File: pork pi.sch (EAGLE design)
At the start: 27 parts, among them J1 SJ-2523-SMT-TR, U1 A13

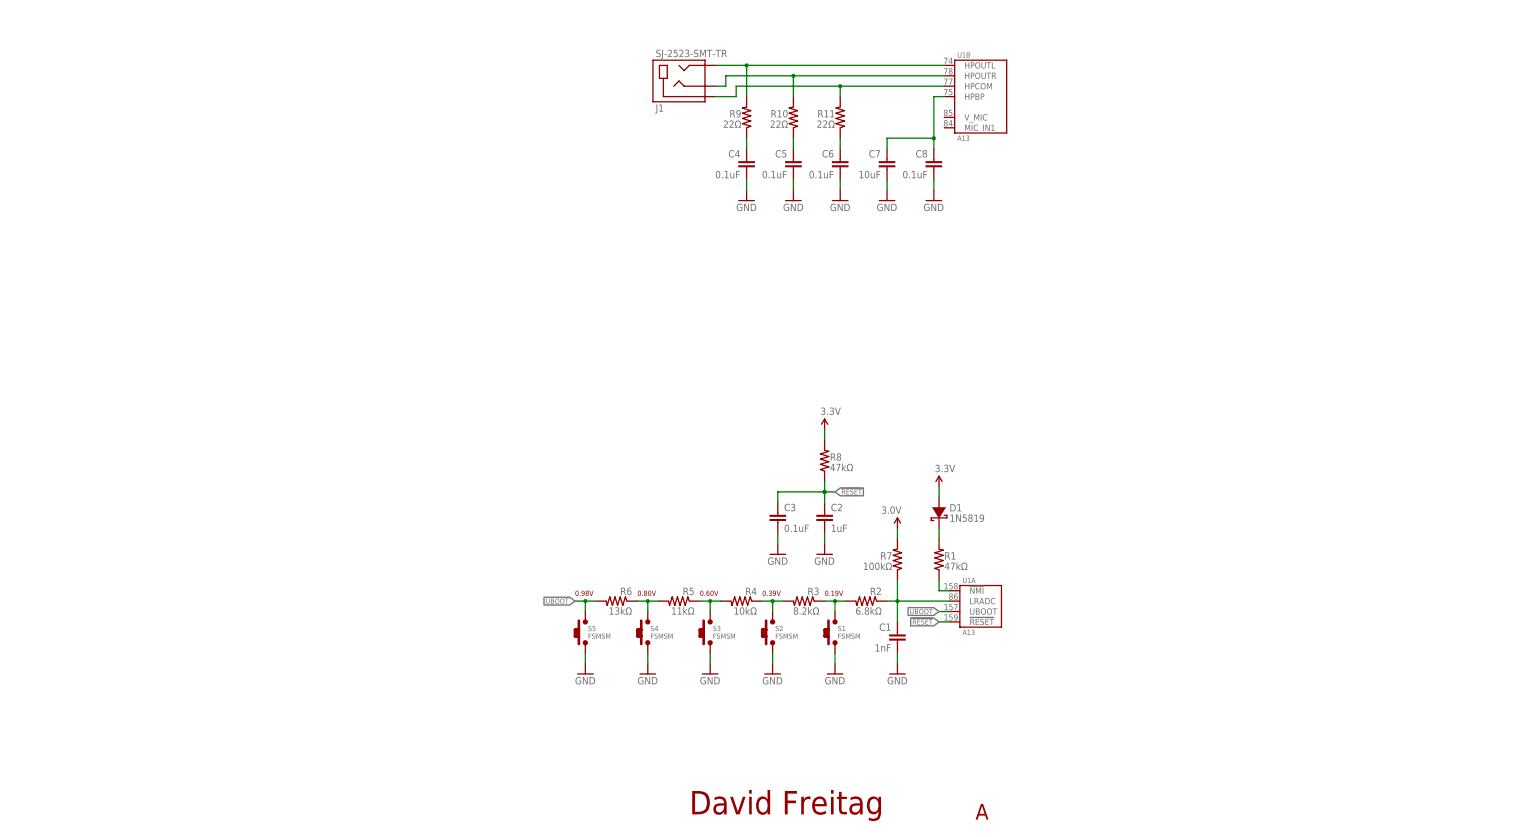
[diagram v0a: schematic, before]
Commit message: Schematic update
Added other gates for U1
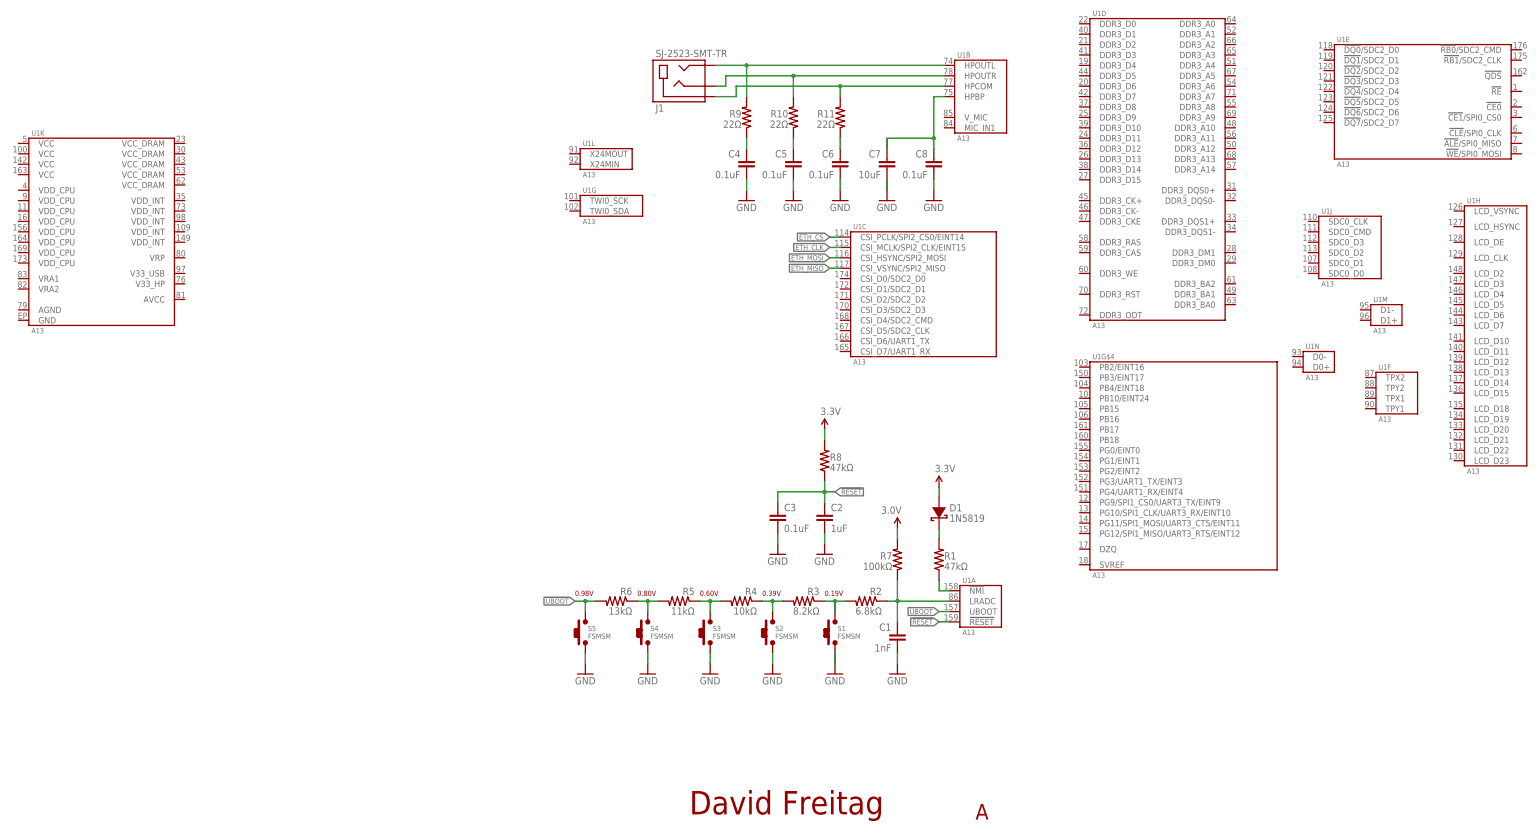
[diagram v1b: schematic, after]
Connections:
- new net ETH_CLK: U1C.CSI_MCLK/SPI2_CLK/EINT15
- new net ETH_CS: U1C.CSI_PCLK/SPI2_CS0/EINT14
- new net ETH_MISO: U1C.CSI_VSYNC/SPI2_MISO
- new net ETH_MOSI: U1C.CSI_HSYNC/SPI2_MOSI
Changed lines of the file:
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@@
 <instance part="GND12" gate="1" x="232.41" y="161.29"/>
 <instance part="GND13" gate="1" x="243.84" y="161.29"/>
+<instance part="U1" gate="C" x="241.3" y="138.43"/>
+<instance part="U1" gate="D" x="298.45" y="168.91"/>
+<instance part="U1" gate="G$4" x="304.8" y="96.52"/>
+<instance part="U1" gate="G" x="165.1" y="160.02"/>
+<instance part="U1" gate="H" x="381" y="128.27"/>
+<instance part="U1" gate="E" x="363.22" y="185.42"/>
+<instance part="U1" gate="L" x="163.83" y="171.45"/>
+<instance part="U1" gate="K" x="40.64" y="153.67"/>
+<instance part="U1" gate="F" x="356.87" y="114.3"/>
+<instance part="U1" gate="J" x="345.44" y="149.86"/>
+<instance part="U1" gate="N" x="337.82" y="121.92"/>
+<instance part="U1" gate="M" x="354.33" y="133.35"/>
 </instances>
 <busses>
@@
 </segment>
 </net>
+<net name="ETH_CS" class="0">
+<segment>
+<pinref part="U1" gate="C" pin="CSI_PCLK/SPI2_CS0/EINT14"/>
+<wire x1="220.98" y1="152.4" x2="218.44" y2="152.4" width="0.1524" layer="91"/>
+<label x="218.44" y="152.4" size="1.27" layer="95" rot="R180" xref="yes"/>
+</segment>
+</net>
+<net name="ETH_CLK" class="0">
+<segment>
+<pinref part="U1" gate="C" pin="CSI_MCLK/SPI2_CLK/EINT15"/>
+<wire x1="220.98" y1="149.86" x2="218.44" y2="149.86" width="0.1524" layer="91"/>
+<label x="218.44" y="149.86" size="1.27" layer="95" rot="R180" xref="yes"/>
+</segment>
+</net>
+<net name="ETH_MOSI" class="0">
+<segment>
+<pinref part="U1" gate="C" pin="CSI_HSYNC/SPI2_MOSI"/>
+<wire x1="220.98" y1="147.32" x2="218.44" y2="147.32" width="0.1524" layer="91"/>
+<label x="218.44" y="147.32" size="1.27" layer="95" rot="R180" xref="yes"/>
+</segment>
+</net>
+<net name="ETH_MISO" class="0">
+<segment>
+<pinref part="U1" gate="C" pin="CSI_VSYNC/SPI2_MISO"/>
+<wire x1="220.98" y1="144.78" x2="218.44" y2="144.78" width="0.1524" layer="91"/>
+<label x="218.44" y="144.78" size="1.27" layer="95" rot="R180" xref="yes"/>
+</segment>
+</net>
